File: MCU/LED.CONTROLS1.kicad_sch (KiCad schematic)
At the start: 21 parts, among them U2 LM5012DDAR, U5 HHG1D-1, U7 AMC1301DWVR

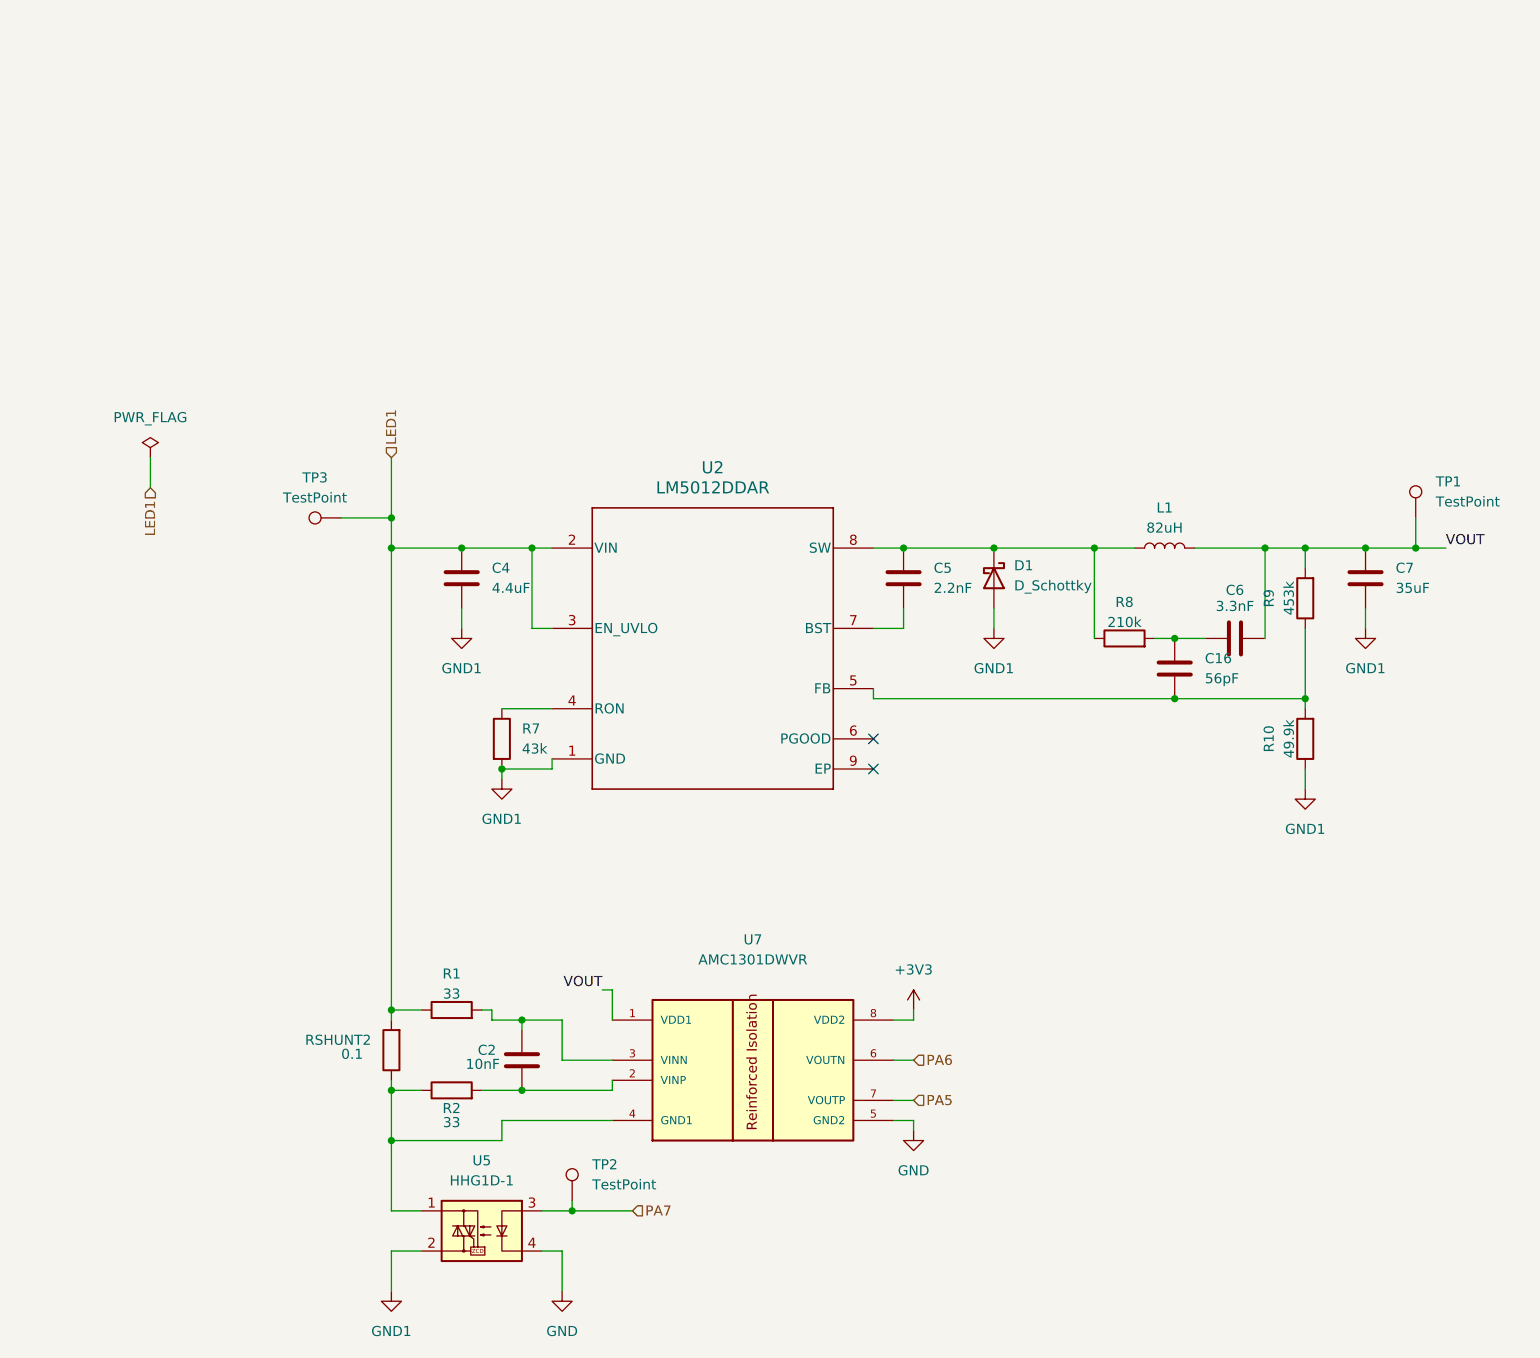
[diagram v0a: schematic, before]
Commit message: Centralized isolation amp power source. Corrected STM32 pins.
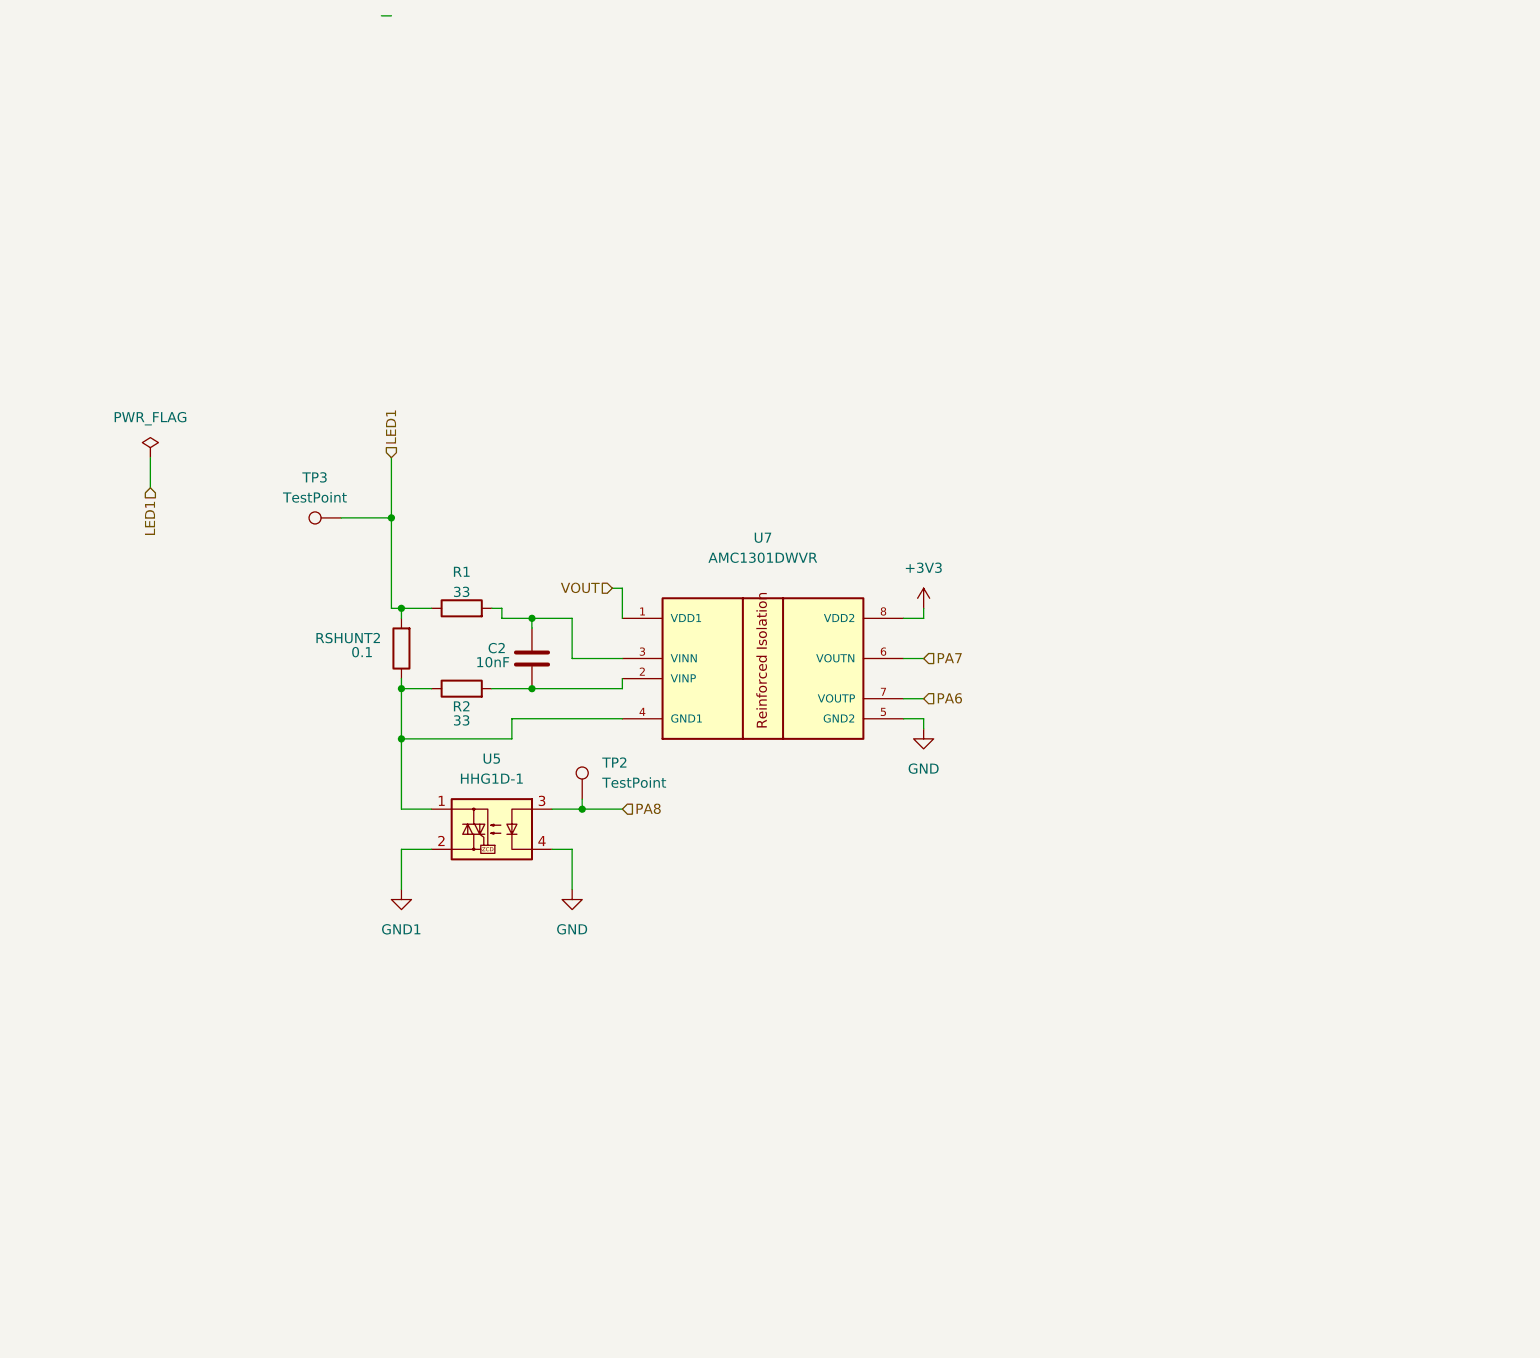
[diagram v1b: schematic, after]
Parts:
- removed C16: 56pF, symbol Device:C
- removed C4: 4.4uF, symbol Device:C
- removed C5: 2.2nF, symbol Device:C
- removed C6: 3.3nF, symbol Device:C
- removed C7: 35uF, symbol Device:C
- removed D1: D_Schottky, symbol Device:D_Schottky
- removed L1: 82uH, symbol Device:L
- removed R10: 49.9k, Resistor_SMD:R_1812_4532Metric_Pad1.30x3.40mm_HandSolder, symbol Device:R
- removed R7: 43k, symbol Device:R
- removed R8: 210k, Resistor_SMD:R_1812_4532Metric_Pad1.30x3.40mm_HandSolder, symbol Device:R
- removed R9: 453k, Resistor_SMD:R_1812_4532Metric_Pad1.30x3.40mm_HandSolder, symbol Device:R
- removed TP1: TestPoint, symbol Connector:TestPoint
- removed U2: LM5012DDAR, DDA0008E-IPC_A, symbol LM 5012 Buck Converter:LM5012DDAR
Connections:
- net PA5 is gone; now on net PA6: U7.7 (VOUTP)
- net PA6: no longer U7.6 (VOUTN)
- net PA7: now also U7.6 (VOUTN); no longer TP2.1, U5.3
- new net PA8: TP2.1, U5.3
- no-connect marks 2 -> 0
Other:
- moved on the sheet: C2, R1, R2, RSHUNT2, TP2, U5, U7

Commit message: Assigned footprints and added RTD
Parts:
- C2: footprint (none) -> Capacitor_SMD:C_1206_3216Metric
- TP2: value TestPoint -> LED1_MCU_CT; footprint (none) -> TestPoint:TestPoint_Pad_1.5x1.5mm
- TP3: value TestPoint -> Post_LED1_Test; footprint (none) -> TestPoint:TestPoint_Pad_2.0x2.0mm
- renumbered RSHUNT2 to RSHUNT1
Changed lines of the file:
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@@
 			)
 		)
-		(property "Datasheet" "~"
+		(property "Datasheet" "https://www.yageogroup.com/content/datasheet/asset/file/PYU-RC_GROUP_51_ROHS_L"
 			(at 127 58.42 0)
 			(effects
@@
 			)
 		)
-		(property "Description" "Resistor"
+		(property "Description" "33 Ohms ±1% 0.063W, 1/16W Chip TR Resistor 0402 (1005 Metric) Moisture Resistant Thick Film"
 			(at 127 58.42 0)
 			(effects
@@
 			)
 		)
-		(property "Footprint" ""
+		(property "Footprint" "Capacitor_SMD:C_1206_3216Metric"
 			(at 136.8552 68.58 0)
 			(effects
@@
 			)
 		)
-		(property "Datasheet" "~"
+		(property "Datasheet" "https://www.yageogroup.com/content/Resource%20Library/Datasheet/UPY-NP0X7R_MV_100-TO-630V.pdf"
 			(at 135.89 64.77 0)
 			(effects
@@
 			)
 		)
-		(property "Description" "Unpolarized capacitor"
+		(property "Description" "10000 pF ±5% 250V Ceramic Capacitor TR X7R 1206 (3216 Metric)"
 			(at 135.89 64.77 0)
 			(effects
@@
 			)
 		)
-		(property "Value" "TestPoint"
+		(property "Value" "LED1_MCU_CT"
 			(at 144.78 80.5179 0)
 			(effects
@@
 			)
 		)
-		(property "Footprint" ""
+		(property "Footprint" "TestPoint:TestPoint_Pad_1.5x1.5mm"
 			(at 147.32 82.55 0)
 			(effects
@@
 		(dnp no)
 		(property "Reference" "R2"
-			(at 127 70.866 90)
+			(at 127 64.008 90)
 			(effects
 				(font
@@
 		)
 		(property "Value" "33"
-			(at 127 72.644 90)
+			(at 127 66.548 90)
 			(effects
 				(font
@@
 			)
 		)
-		(property "Datasheet" "~"
+		(property "Datasheet" "https://www.yageogroup.com/content/datasheet/asset/file/PYU-RC_GROUP_51_ROHS_L"
 			(at 127 68.58 0)
 			(effects
@@
 			)
 		)
-		(property "Description" "Resistor"
+		(property "Description" "33 Ohms ±1% 0.063W, 1/16W Chip TR Resistor 0402 (1005 Metric) Moisture Resistant Thick Film"
 			(at 127 68.58 0)
 			(effects
@@
 		(on_board yes)
 		(dnp no)
-		(property "Reference" "RSHUNT2"
+		(property "Reference" "RSHUNT1"
 			(at 108.458 62.23 0)
 			(effects
@@
 			)
 		)
-		(property "Datasheet" "~"
+		(property "Datasheet" "https://industrial.panasonic.com/cdbs/www-data/pdf/RDN0000/AOA0000C313.pdf"
 			(at 119.38 63.5 0)
 			(effects
@@
 			)
 		)
-		(property "Description" "Resistor"
+		(property "Description" "RES TR 0.1 OHM 1% 1/10W 0603"
 			(at 119.38 63.5 0)
 			(effects
@@
 			(project "MCU"
 				(path "/56b3f3ef-07ec-480e-b5f8-5a7fd51b01f6/ebe2158f-a1b2-4452-963c-f041e3feae05"
-					(reference "RSHUNT2")
+					(reference "RSHUNT1")
 					(unit 1)
 				)
@@
 			)
 		)
-		(property "Value" "TestPoint"
+		(property "Value" "Post_LED1_Test"
 			(at 108.458 44.45 90)
 			(effects
@@
 			)
 		)
-		(property "Footprint" ""
+		(property "Footprint" "TestPoint:TestPoint_Pad_2.0x2.0mm"
 			(at 111.76 41.91 0)
 			(effects

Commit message: Finalized schematic and started layout
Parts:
- removed R2: 33, Resistor_SMD:R_1812_4532Metric_Pad1.30x3.40mm_HandSolder, symbol Device:R
- removed U7: AMC1301DWVR, AMC1301DWVR:SOIC127P1150X280-8N, symbol AMC1301:AMC1301DWVR
- added C2, C5, C9: 100nF, Capacitor_SMD:C_0201_0603Metric_Pad0.64x0.40mm_HandSolder, symbol Device:C
- added C3: 1uF, Capacitor_SMD:C_0201_0603Metric_Pad0.64x0.40mm_HandSolder, symbol Device:C
- added C4, C6, C7, C8: 1nF, Capacitor_SMD:C_0201_0603Metric_Pad0.64x0.40mm_HandSolder, symbol Device:C
- added R3: 10, Resistor_SMD:R_0603_1608Metric_Pad0.98x0.95mm_HandSolder, symbol Device:R
- added R4: 0, Resistor_SMD:R_0603_1608Metric_Pad0.98x0.95mm_HandSolder, symbol Device:R
- added R5: 47k, Resistor_SMD:R_0603_1608Metric_Pad0.98x0.95mm_HandSolder, symbol Device:R
- added U4: AMC3302QDWERQ1, AMC3302-Q1 Isolated Amplifier:SOIC-3302DWERQ1_TEX, symbol AMC3302-Q1 Isolated Amp:AMC3302QDWERQ1
- R2: renamed from R1; value 33 -> 10; footprint Resistor_SMD:R_1812_4532Metric_Pad1.30x3.40mm_HandSolder -> Resistor_SMD:R_0603_1608Metric_Pad0.98x0.95mm_HandSolder
- RSHUNT1: value 0.1 -> 0.04; footprint Resistor_SMD:R_1812_4532Metric_Pad1.30x3.40mm_HandSolder -> Resistor_SMD:R_2512_6332Metric_Pad1.40x3.35mm_HandSolder
- renumbered C2 to C1, TP3 to TP1, U5 to U3
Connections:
- net +3V3: now also C7.1, C8.1, R5.2, U4.12 (VDD)
- net GND: now also C7.2, C8.2, C9.2, U4.13 (LDO_OUT), U4.15 (DCDC_GND), U4.9 (GND)
- net at C1.1, R2.2: now also U4.6 (INP)
- net at C1.2: now also R3.2, U4.7 (INN)
- net at RSHUNT1.1, U3.1: now also C2.2, C3.2, C4.2, C5.2, C6.2, R3.1, U4.2 (DCDC_HGND), U4.8 (HGND)
- net LED1 renamed LED_IN
- net PA8: no longer names the net of TP2.1, U3.3
- net PA8: now also R4.1
- new net: C3.1, C4.1, C5.1, U4.1 (DCDC_OUT), U4.3 (HLDO_IN)
- new net: C9.1, U4.16 (DCDC_IN)
- new net: C2.1, C6.1, U4.5 (HLDO_OUT)
- new net CTRL: R4.2
- new net DIAG: R5.1, U4.14 (DIAG)
- new net VOUTN: U4.10 (OUTN)
- new net VOUTP: U4.11 (OUTP)
- no-connect marks 0 -> 1
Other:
- moved on the sheet: C1, R2, RSHUNT1, TP1, TP2, U3

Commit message: MCU Layout V1
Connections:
- net CTRL: now also R4.1; no longer R4.2
- net at TP2.1, U3.3: now also R4.2; no longer R4.1
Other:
- moved on the sheet: R4
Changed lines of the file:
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@@
 	(symbol
 		(lib_id "Device:R")
-		(at 134.62 118.11 90)
+		(at 134.62 118.11 270)
+		(mirror x)
 		(unit 1)
 		(exclude_from_sim no)
@@
 		(on_board yes)
 		(dnp no)
-		(fields_autoplaced yes)
 		(property "Reference" "R4"
 			(at 134.62 111.76 90)

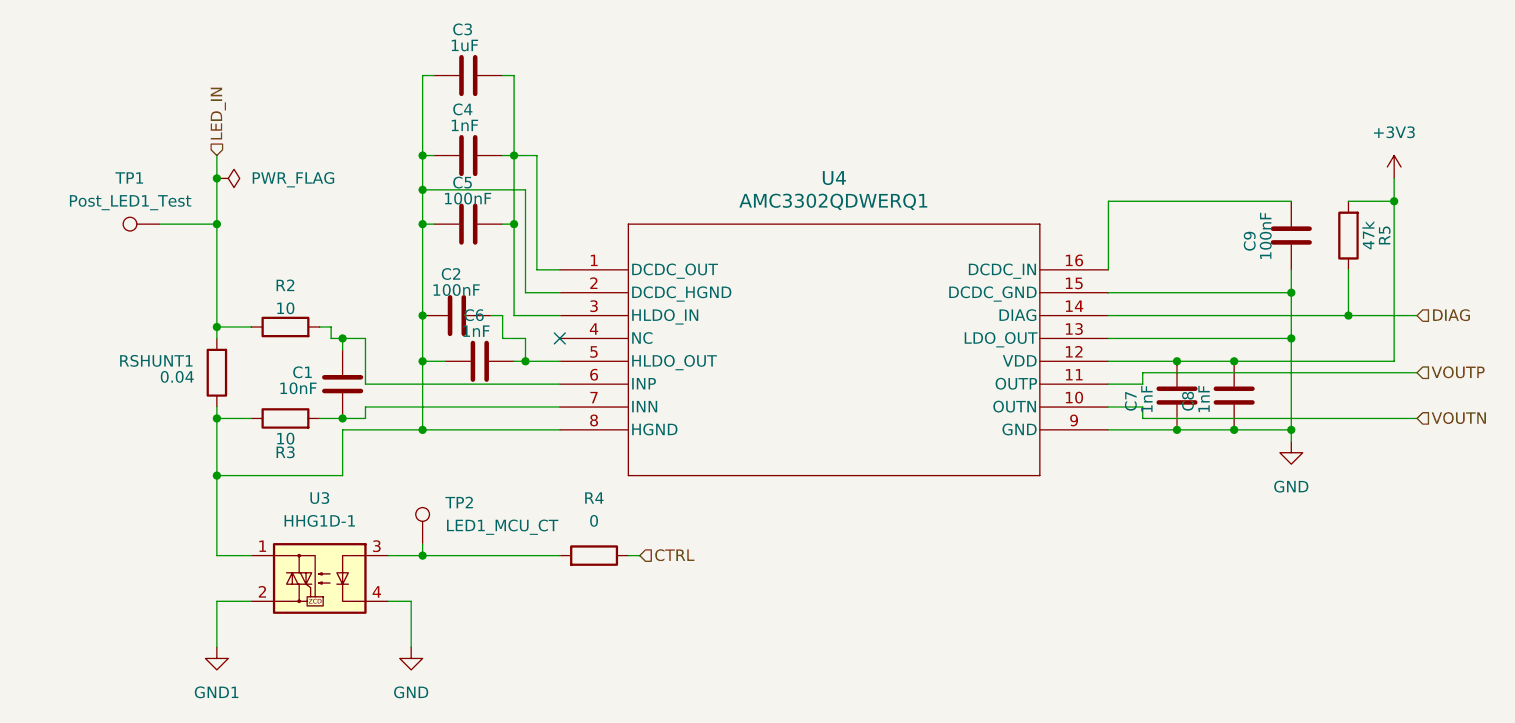
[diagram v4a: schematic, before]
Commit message: Adjusted trace widths. Added ferrite beads. Changed connectors to fit new trace widths. Added +3V3 fill zone in B.Cu. Fixed silkscreen placements.
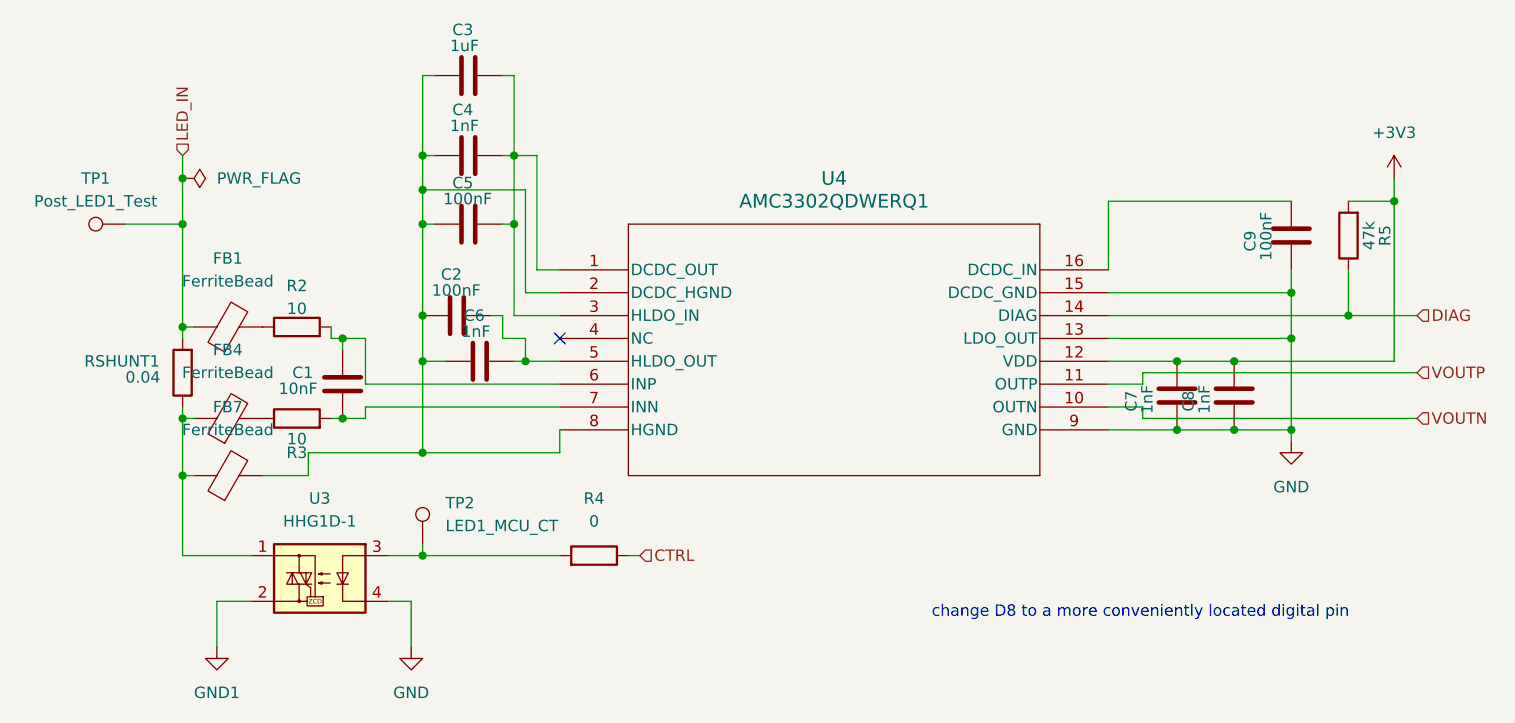
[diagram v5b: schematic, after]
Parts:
- added FB1, FB4, FB7: FerriteBead, Resistor_SMD:R_0402_1005Metric_Pad0.72x0.64mm_HandSolder, symbol Device:FerriteBead
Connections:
- net LED_IN: now also FB1.1; no longer R2.1
- net at C2.2, C3.2, C4.2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: now also FB7.2; no longer R3.1, RSHUNT1.1, U3.1
- new net: FB1.2, R2.1
- new net: FB4.1, FB7.1, RSHUNT1.1, U3.1
- new net: FB4.2, R3.1
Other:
- note added: "change D8 to a more conveniently located digital pin"
- moved on the sheet: R2, R3, RSHUNT1, TP1
